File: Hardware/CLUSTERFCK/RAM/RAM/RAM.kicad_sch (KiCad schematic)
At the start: 40 parts, among them J1 Conn_02x10_Counter_Clockwise, J2 Conn_02x06_Counter_Clockwise, J3 Conn_02x08_Counter_Clockwise, J4 Conn_02x10_Counter_Clockwise, J5 Conn_02x06_Counter_Clockwise, J6 Conn_02x08_Counter_Clockwise, U1 74LS245, U10 74HCT164, U11 74LS157, U12 74LS157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

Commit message: 0050 | 5h | Ram module
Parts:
- removed J4: Conn_02x10_Counter_Clockwise, Connector_PinHeader_2.54mm:PinHeader_2x10_P2.54mm_Horizontal, symbol Connector_Generic:Conn_02x10_Counter_Clockwise
- added J7: Conn_02x04_Odd_Even, Connector_PinHeader_2.54mm:PinHeader_2x04_P2.54mm_Horizontal, symbol Connector_Generic:Conn_02x04_Odd_Even
- added J8: Conn_02x06_Odd_Even, Connector_PinHeader_2.54mm:PinHeader_2x06_P2.54mm_Horizontal, symbol Connector_Generic:Conn_02x06_Odd_Even
- C1, C10, C11, C12, C13, C14, C2, C3, C4, C5, C6, C7, C8, C9: footprint (none) -> Capacitor_SMD:C_0805_2012Metric_Pad1.15x1.40mm_HandSolder
- J2: footprint Connector_PinHeader_2.54mm:PinHeader_2x06_P2.54mm_Horizontal -> Connector_PinHeader_2.54mm:PinHeader_2x06_P2.54mm_Vertical
- J3: footprint Connector_PinHeader_2.54mm:PinHeader_2x08_P2.54mm_Horizontal -> Connector_PinHeader_2.54mm:PinHeader_2x08_P2.54mm_Vertical
- U1, U14, U2: footprint (none) -> Package_SO:TSSOP-20_4.4x6.5mm_P0.65mm
- U10, U4, U5, U9: footprint (none) -> Package_SO:SOIC-14_3.9x8.7mm_P1.27mm
- U11, U12, U13: footprint (none) -> Package_SO:SOIC-16_3.9x9.9mm_P1.27mm
- U29, U3, U6: footprint (none) -> Package_SO:SOIC-14W_7.5x9mm_P1.27mm
- U29: footprint Package_DIP:DIP-14_W7.62mm_Socket_LongPads -> Package_SO:SOIC-14W_7.5x9mm_P1.27mm
- U7, U8: footprint (none) -> Package_DIP:DIP-24_W15.24mm_Socket_LongPads
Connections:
- net ADDR0: now also J8.1 (Pin_1)
- net ADDR1: now also J8.3 (Pin_3)
- net ADDR10: now also J8.10 (Pin_10)
- net ADDR11: now also J8.12 (Pin_12)
- net ADDR2: now also J8.5 (Pin_5)
- net ADDR3: now also J8.7 (Pin_7)
- net ADDR4: now also J8.9 (Pin_9)
- net ADDR5: now also J8.11 (Pin_11)
- net ADDR6: now also J8.2 (Pin_2)
- net ADDR7: now also J8.4 (Pin_4)
- net ADDR8: now also J8.6 (Pin_6)
- net ADDR9: now also J8.8 (Pin_8)
- net DATA0: now also J7.1 (Pin_1)
- net DATA1: now also J7.3 (Pin_3)
- net DATA2: now also J7.5 (Pin_5)
- net DATA3: now also J7.7 (Pin_7)
- net DATA4: now also J7.2 (Pin_2)
- net DATA5: now also J7.4 (Pin_4)
- net DATA6: now also J7.6 (Pin_6)
- net DATA7: now also J7.8 (Pin_8)
- no-connect marks 31 -> 24

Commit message: UNSTABLE PUSH! RAM NOT WIRED!
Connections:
- net MEMADDR0: now also J2.11 (Pin_11), J5.11 (Pin_11); no longer J2.1 (Pin_1), J5.1 (Pin_1)
- net MEMADDR1: now also J2.12 (Pin_12), J5.12 (Pin_12); no longer J2.2 (Pin_2), J5.2 (Pin_2)
- net MEMADDR10: now also J2.1 (Pin_1), J5.1 (Pin_1); no longer J2.11 (Pin_11), J5.11 (Pin_11)
- net MEMADDR11: now also J2.2 (Pin_2), J5.2 (Pin_2); no longer J2.12 (Pin_12), J5.12 (Pin_12)
- net MEMADDR2: now also J2.9 (Pin_9), J5.9 (Pin_9); no longer J2.3 (Pin_3), J5.3 (Pin_3)
- net MEMADDR3: now also J2.10 (Pin_10), J5.10 (Pin_10); no longer J2.4 (Pin_4), J5.4 (Pin_4)
- net MEMADDR4: now also J2.7 (Pin_7), J5.7 (Pin_7); no longer J2.5 (Pin_5), J5.5 (Pin_5)
- net MEMADDR5: now also J2.8 (Pin_8), J5.8 (Pin_8); no longer J2.6 (Pin_6), J5.6 (Pin_6)
- net MEMADDR6: now also J2.5 (Pin_5), J5.5 (Pin_5); no longer J2.7 (Pin_7), J5.7 (Pin_7)
- net MEMADDR7: now also J2.6 (Pin_6), J5.6 (Pin_6); no longer J2.8 (Pin_8), J5.8 (Pin_8)
- net MEMADDR8: now also J2.3 (Pin_3), J5.3 (Pin_3); no longer J2.9 (Pin_9), J5.9 (Pin_9)
- net MEMADDR9: now also J2.4 (Pin_4), J5.4 (Pin_4); no longer J2.10 (Pin_10), J5.10 (Pin_10)
- net RAMOBUS0: now also J3.15 (Pin_15), J6.15 (Pin_15); no longer J3.1 (Pin_1), J6.1 (Pin_1)
- net RAMOBUS1: now also J3.16 (Pin_16), J6.16 (Pin_16); no longer J3.2 (Pin_2), J6.2 (Pin_2)
- net RAMOBUS10: now also J3.5 (Pin_5), J6.5 (Pin_5); no longer J3.11 (Pin_11), J6.11 (Pin_11)
- net RAMOBUS11: now also J3.6 (Pin_6), J6.6 (Pin_6); no longer J3.12 (Pin_12), J6.12 (Pin_12)
- net RAMOBUS12: now also J3.3 (Pin_3), J6.3 (Pin_3); no longer J3.13 (Pin_13), J6.13 (Pin_13)
- net RAMOBUS13: now also J3.4 (Pin_4), J6.4 (Pin_4); no longer J3.14 (Pin_14), J6.14 (Pin_14)
- net RAMOBUS14: now also J3.1 (Pin_1), J6.1 (Pin_1); no longer J3.15 (Pin_15), J6.15 (Pin_15)
- net RAMOBUS15: now also J3.2 (Pin_2), J6.2 (Pin_2); no longer J3.16 (Pin_16), J6.16 (Pin_16)
- net RAMOBUS2: now also J3.13 (Pin_13), J6.13 (Pin_13); no longer J3.3 (Pin_3), J6.3 (Pin_3)
- net RAMOBUS3: now also J3.14 (Pin_14), J6.14 (Pin_14); no longer J3.4 (Pin_4), J6.4 (Pin_4)
- net RAMOBUS4: now also J3.11 (Pin_11), J6.11 (Pin_11); no longer J3.5 (Pin_5), J6.5 (Pin_5)
- net RAMOBUS5: now also J3.12 (Pin_12), J6.12 (Pin_12); no longer J3.6 (Pin_6), J6.6 (Pin_6)
- net RAMOBUS6: now also J3.9 (Pin_9), J6.9 (Pin_9); no longer J3.7 (Pin_7), J6.7 (Pin_7)
- net RAMOBUS7: now also J3.10 (Pin_10), J6.10 (Pin_10); no longer J3.8 (Pin_8), J6.8 (Pin_8)
- net RAMOBUS8: now also J3.7 (Pin_7), J6.7 (Pin_7); no longer J3.9 (Pin_9), J6.9 (Pin_9)
- net RAMOBUS9: now also J3.8 (Pin_8), J6.8 (Pin_8); no longer J3.10 (Pin_10), J6.10 (Pin_10)

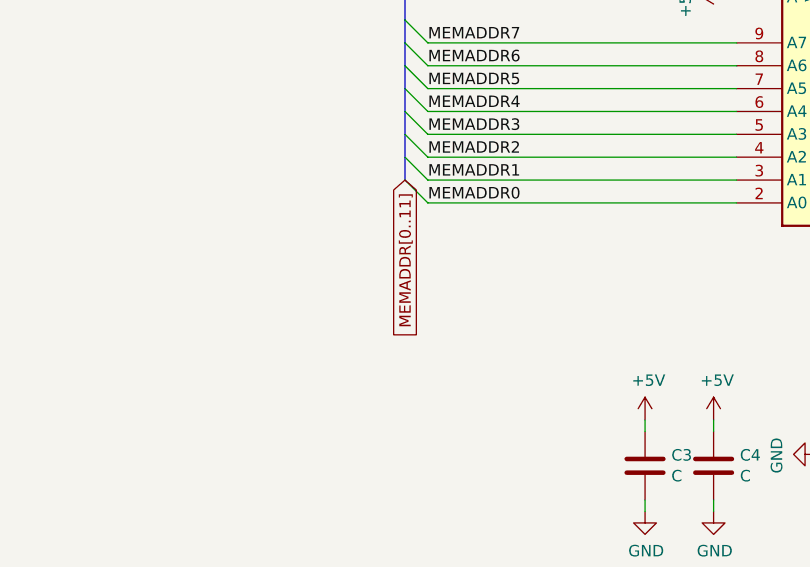
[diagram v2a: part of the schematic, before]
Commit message: 0070 | 6h | completely rerouted RAM
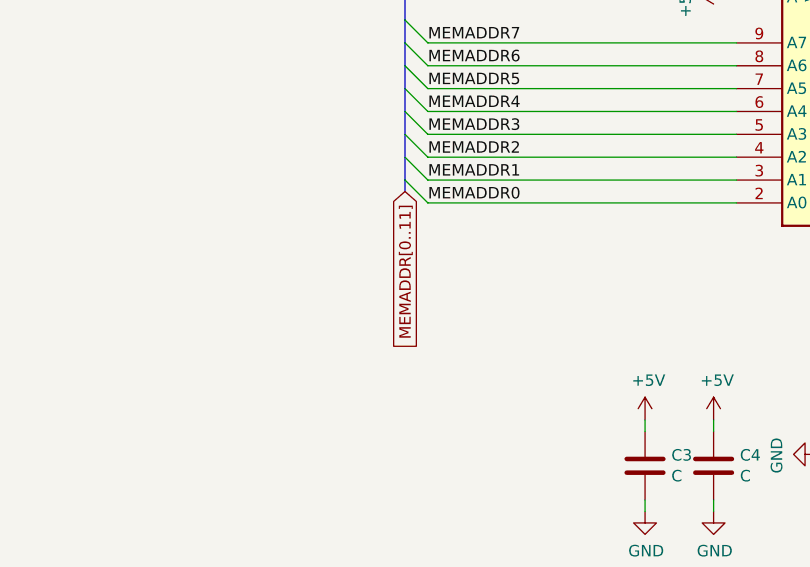
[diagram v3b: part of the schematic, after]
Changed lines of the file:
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@@
   (junction (at 473.71 313.69) (diameter 1.016) (color 0 0 0 0))
   (junction (at 511.175 144.78) (diameter 1.016) (color 0 0 0 0))
-  (no_connect (at 127 142.24))
-  (no_connect (at 198.12 289.56))
-  (no_connect (at 127 147.32))
-  (no_connect (at 35.56 383.54))
-  (no_connect (at 516.89 234.95))
-  (no_connect (at 213.36 299.72))
-  (no_connect (at 213.36 302.26))
-  (no_connect (at 134.62 218.44))
-  (no_connect (at 198.12 292.1))
   (no_connect (at 210.82 292.1))
+  (no_connect (at 213.36 302.26))
+  (no_connect (at 511.81 234.95))
+  (no_connect (at 213.36 299.72))
+  (no_connect (at 132.08 218.44))
+  (no_connect (at 198.12 294.64))
+  (no_connect (at 516.89 234.95))
   (no_connect (at 35.56 365.76))
   (no_connect (at 127 144.78))
-  (no_connect (at 511.81 234.95))
-  (no_connect (at 142.24 218.44))
-  (no_connect (at 519.43 234.95))
+  (no_connect (at 127 147.32))
+  (no_connect (at 127 142.24))
+  (no_connect (at 134.62 218.44))
   (no_connect (at 198.12 297.18))
-  (no_connect (at 35.56 374.65))
-  (no_connect (at 127 152.4))
+  (no_connect (at 519.43 234.95))
+  (no_connect (at 139.7 218.44))
   (no_connect (at 137.16 218.44))
+  (no_connect (at 198.12 289.56))
+  (no_connect (at 142.24 218.44))
   (no_connect (at 127 149.86))
-  (no_connect (at 198.12 294.64))
-  (no_connect (at 132.08 218.44))
-  (no_connect (at 139.7 218.44))
+  (no_connect (at 35.56 374.65))
   (no_connect (at 514.35 234.95))
+  (no_connect (at 198.12 292.1))
+  (no_connect (at 35.56 383.54))
+  (no_connect (at 127 152.4))
   (bus_entry (at 55.245 27.305) (size -2.54 2.54)
     (stroke (width 0.1524) (type solid) (color 0 0 0 0))
@@
     (stroke (width 0) (type solid) (color 0 0 0 0))
   )
+  (bus (pts (xy 80.01 198.12) (xy 80.01 199.39))
+    (stroke (width 0) (type solid) (color 0 0 0 0))
+  )
   (bus (pts (xy 127 -1.27) (xy 127 6.35))
     (stroke (width 0) (type solid) (color 0 0 0 0))
@@
     (effects (font (size 1.27 1.27)) (justify right bottom))
   )
-  (global_label "MEMADDR[0..11]" (shape input) (at 80.01 198.12 270)    (property "Intersheet References" "${INTERSHEET_REFS}" (id 0) (at 0 0 0)
+  (global_label "MEMADDR[0..11]" (shape input) (at 80.01 199.39 270)    (property "Intersheet References" "${INTERSHEET_REFS}" (id 0) (at 0 1.27 0)
       (effects (font (size 1.27 1.27)) hide)
     )
